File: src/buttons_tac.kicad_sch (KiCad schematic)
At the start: 0 parts

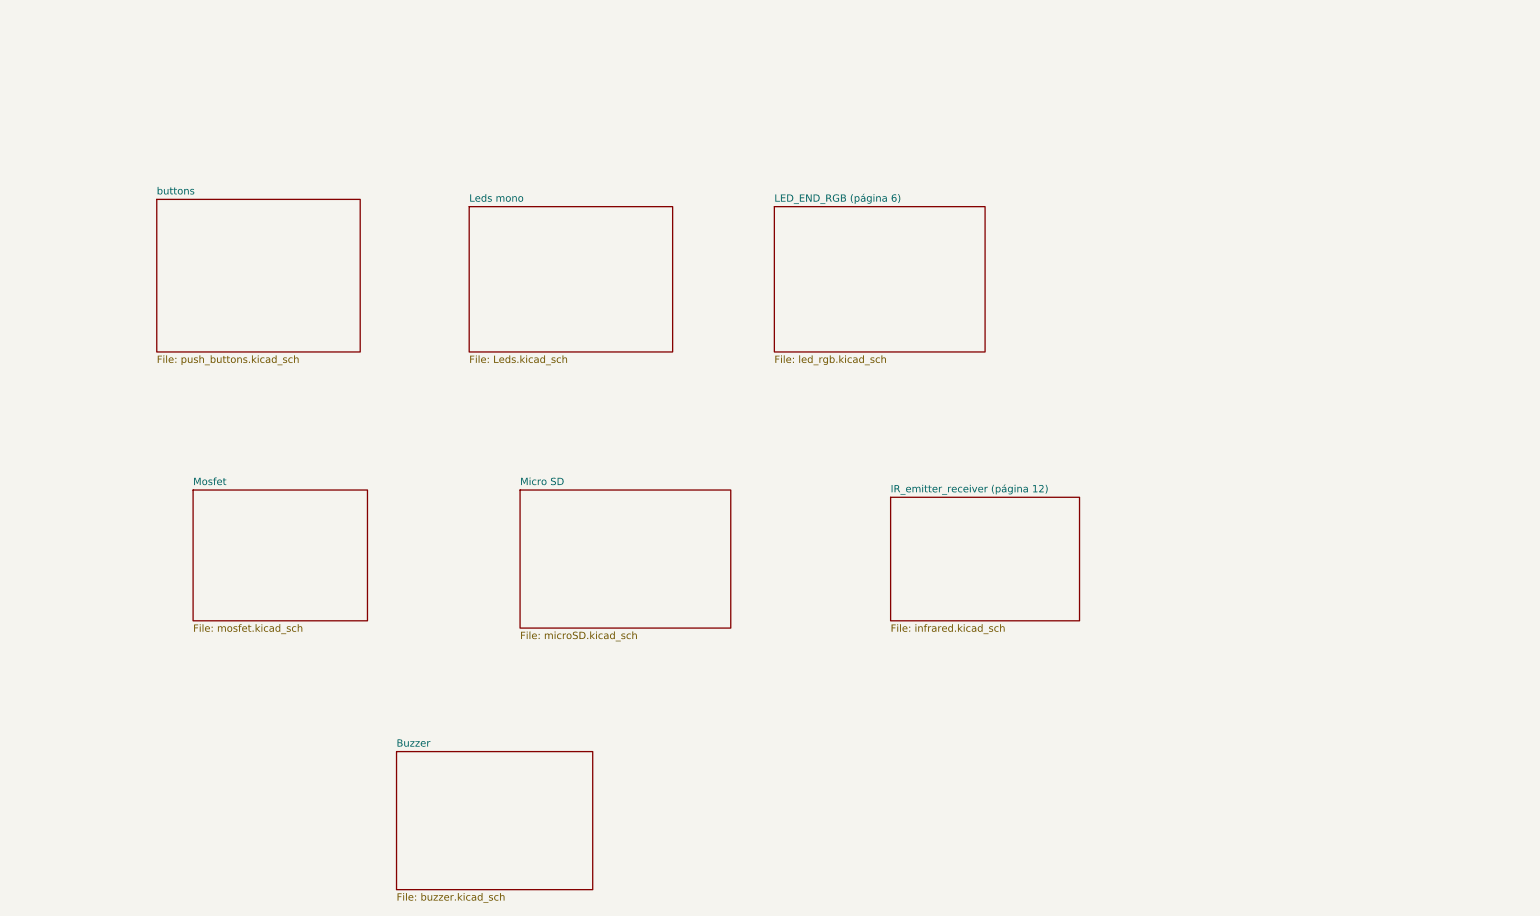
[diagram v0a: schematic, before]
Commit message: fix: Consertando paginação e refact da Tela_OLED
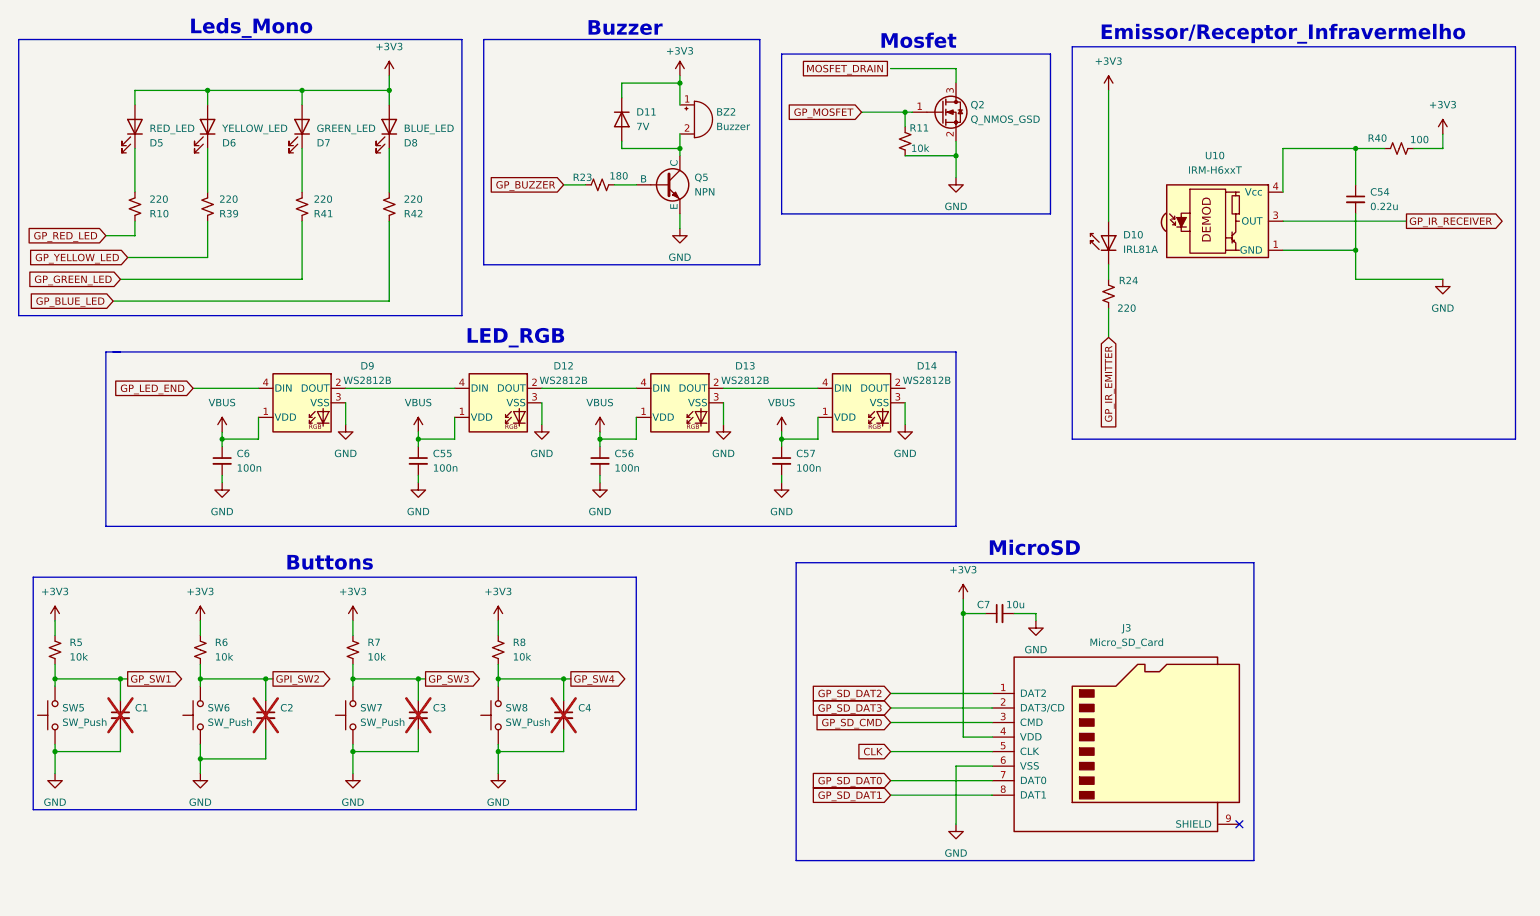
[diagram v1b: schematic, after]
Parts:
- added BZ2: Buzzer, symbol Device:Buzzer
- added C1, C2, C3, C4: ~, Capacitor_SMD:C_0402_1005Metric, symbol Device:C_Small
- added C54: 0.22u, Capacitor_SMD:C_0402_1005Metric, symbol Device:C_Small
- added C55, C56, C57, C6: 100n, Capacitor_SMD:C_0402_1005Metric, symbol Device:C_Small
- added C7: 10u, Capacitor_SMD:C_0402_1005Metric, symbol Device:C_Small
- added D10: IRL81A, LED_THT:LED_SideEmitter_Rectangular_W4.5mm_H1.6mm, symbol LED:IRL81A
- added D11: 7V, Diode_SMD:D_SOD-523, symbol Diode:1N4148WT
- added D12, D13, D14, D9: WS2812B, LED_SMD:LED_WS2812B_PLCC4_5.0x5.0mm_P3.2mm, symbol LED:WS2812B
- added D5: RED_LED, LED_SMD:LED_0603_1608Metric, symbol Device:LED
- added D6: YELLOW_LED, LED_SMD:LED_0603_1608Metric, symbol Device:LED
- added D7: GREEN_LED, LED_SMD:LED_0603_1608Metric, symbol Device:LED
- added D8: BLUE_LED, LED_SMD:LED_0603_1608Metric, symbol Device:LED
- added J3: Micro_SD_Card, symbol Connector:Micro_SD_Card
- added Q2: Q_NMOS_GSD, symbol Transistor_FET:Q_NMOS_GSD
- added Q5: NPN, symbol Simulation_SPICE:NPN
- added R10, R39, R41, R42: 220, Resistor_SMD:R_0402_1005Metric, symbol Device:R_Small_US
- added R11, R5, R6, R7, R8: 10k, Resistor_SMD:R_0402_1005Metric, symbol Device:R_Small_US
- added R23: 180, symbol Device:R_Small_US
- added R24: 220, symbol Device:R_Small_US
- added R40: 100, Resistor_SMD:R_0402_1005Metric, symbol Device:R_Small_US
- added SW5, SW6, SW7, SW8: SW_Push, symbol Switch:SW_Push
- added U10: IRM-H6xxT, OptoDevice:Everlight_IRM-H6xxT, symbol Interface_Optical:IRM-H6xxT
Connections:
- new net: BZ2.2 (-), D11.2 (A), Q5.1 (C)
- new net: D12.2 (DOUT), D13.4 (DIN)
- new net: D12.4 (DIN), D9.2 (DOUT)
- new net: D7.1 (K), R41.2
- new net: D6.1 (K), R39.2
- new net: D5.1 (K), R10.2
- new net: D13.2 (DOUT), D14.4 (DIN)
- new net: Q5.2 (B), R23.1
- new net: D8.1 (K), R42.2
- new net: C54.1, R40.1, U10.4 (Vcc)
- new net: D10.1 (K), R24.1
- new net +3V3: BZ2.1 (+), C7.1, D10.2 (A), D11.1 (K), D5.2 (A), D6.2 (A), D7.2 (A), D8.2 (A), J3.4 (VDD), R40.2, R5.1, R6.1, R7.1, R8.1
- new net CLK: J3.5 (CLK)
- new net GND: C1.2, C2.2, C3.2, C4.2, C54.2, C55.2, C56.2, C57.2, C6.2, C7.2, D12.3 (VSS), D13.3 (VSS), D14.3 (VSS), D9.3 (VSS), J3.6 (VSS), Q2.2 (S), Q5.3 (E), R11.2, SW5.1, SW6.1, SW7.1, SW8.1, U10.1 (GND), U10.2 (GND)
- new net GPI_SW2: C2.1, R6.2, SW6.2
- new net GP_BLUE_LED: R42.1
- new net GP_BUZZER: R23.2
- new net GP_GREEN_LED: R41.1
- new net GP_IR_EMITTER: R24.2
- new net GP_IR_RECEIVER: U10.3 (OUT)
- new net GP_LED_END: D9.4 (DIN)
- new net GP_MOSFET: Q2.1 (G), R11.1
- new net GP_RED_LED: R10.1
- new net GP_SD_CMD: J3.3 (CMD)
- new net GP_SD_DAT0: J3.7 (DAT0)
- new net GP_SD_DAT1: J3.8 (DAT1)
- new net GP_SD_DAT2: J3.1 (DAT2)
- new net GP_SD_DAT3: J3.2 (DAT3/CD)
- new net GP_SW1: C1.1, R5.2, SW5.2
- new net GP_SW3: C3.1, R7.2, SW7.2
- new net GP_SW4: C4.1, R8.2, SW8.2
- new net GP_YELLOW_LED: R39.1
- new net VBUS: C55.1, C56.1, C57.1, C6.1, D12.1 (VDD), D13.1 (VDD), D14.1 (VDD), D9.1 (VDD)
- no-connect marks 0 -> 1
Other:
- removed sheet Buzzer
- removed sheet IR_emitter_receiver (página 12)
- removed sheet LED_END_RGB (página 6)
- removed sheet Leds mono
- removed sheet Micro SD
- removed sheet Mosfet
- removed sheet buttons
- note added: "Buttons"
- note added: "Buzzer"
- note added: "Emissor/Receptor_Infravermelho"
- note added: "LED_RGB"
- note added: "Leds_Mono"
- note added: "MicroSD"
- note added: "Mosfet"

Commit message: FEAT: adicionando footprints
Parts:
- BZ2: footprint (none) -> Buzzer_Beeper:Buzzer_12x9.5RM7.6
- SW5, SW6, SW7, SW8: footprint (none) -> Button_Switch_THT:SW_PUSH_6mm
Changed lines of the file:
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@@
 			)
 		)
-		(property "Footprint" ""
+		(property "Footprint" "Button_Switch_THT:SW_PUSH_6mm"
 			(at 43.18 135.89 0)
 			(effects
@@
 			)
 		)
-		(property "Footprint" ""
+		(property "Footprint" "Buzzer_Beeper:Buzzer_12x9.5RM7.6"
 			(at 133.985 29.21 90)
 			(effects
@@
 			)
 		)
-		(property "Footprint" ""
+		(property "Footprint" "Button_Switch_THT:SW_PUSH_6mm"
 			(at 95.25 135.89 0)
 			(effects
@@
 			)
 		)
-		(property "Footprint" ""
+		(property "Footprint" "Button_Switch_THT:SW_PUSH_6mm"
 			(at 69.85 135.89 0)
 			(effects
@@
 			)
 		)
-		(property "Footprint" ""
+		(property "Footprint" "Button_Switch_THT:SW_PUSH_6mm"
 			(at 17.78 135.89 0)
 			(effects
